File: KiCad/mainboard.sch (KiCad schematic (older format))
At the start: 60 parts, among them J1 Arduino_Nano_Header, P1 CONN_02X13, P2 CONN_02X13, P3 USB_B, P4 CONN_01X04, P5 CONN_01X02, P6 CONN_01X02, P7 CONN_01X02, U1 74LS165, U2 74LS165, U3 7400, U4 74LS595, U5 74LS595, U6 74LS595, U7 74LS595

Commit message: some changes and improvments
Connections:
- net GND: now also P3.5 (shield)
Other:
- moved on the sheet: P5, P6, P7

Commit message: added some metainfo
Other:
- note removed: "Podregilo main board"
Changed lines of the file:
@@
 encoding utf-8
 Sheet 1 1
-Title ""
+Title "Podregilo mainboard"
 Date ""
 Rev ""
-Comp ""
+Comp "https://github.com/johannes-mueller/Podregilo"
 Comment1 ""
 Comment2 ""
@@
 	1    0    0    -1
 $EndComp
-Text Notes 8350 7500 2    60   ~ 0
-Podregilo main board
 $Comp
 L GND #PWR07

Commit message: Added four missing LED-resistors and ...
... turned Arduino again. That was necessary because the connector must not be
at the edge of the PCB.
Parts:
- added R52, R53, R54, R55: 1k, Resistors_ThroughHole:Resistor_Horizontal_RM7mm, symbol R
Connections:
- net at P2.17 (P17): now also R55.2; no longer J1.14 (D11/MOSI)
- net at P2.19 (P19): now also R54.2; no longer J1.13 (D10/SS)
- net at P2.21 (P21): now also R53.2; no longer J1.12 (D9/0C1)
- net at P2.23 (P23): now also R52.2; no longer J1.11 (D8/ICP)
- new net: J1.11 (D8/ICP), R52.1
- new net: J1.12 (D9/0C1), R53.1
- new net: J1.13 (D10/SS), R54.1
- new net: J1.14 (D11/MOSI), R55.1
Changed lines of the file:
@@
 	800  6500 1000 6500
 Wire Wire Line
-	800  5100 800  6500
-Wire Wire Line
-	800  6500 800  7550
+	800  5100 800  7550
 Wire Wire Line
 	1000 5100 800  5100
@@
 	750  5400 1000 5400
 Wire Wire Line
-	750  5400 750  6800
-Wire Wire Line
-	750  6800 750  7600
+	750  5400 750  7600
 Wire Wire Line
 	750  6800 1000 6800
@@
 	4800 2550 4800 750
 Wire Wire Line
-	2200 2550 4250 2550
-Wire Wire Line
-	4250 2550 4800 2550
+	2200 2550 4800 2550
 Wire Wire Line
 	4250 2300 4250 2550
@@
 	4700 2500 4700 650
 Wire Wire Line
-	2350 2500 4400 2500
-Wire Wire Line
-	4400 2500 4700 2500
+	2350 2500 4700 2500
 Wire Wire Line
 	4400 2300 4400 2500
@@
 	7400 1350 7400 3700
 Wire Wire Line
-	5150 1850 5150 2750
-Wire Wire Line
-	5150 2750 5150 3800
+	5150 1850 5150 3800
 Wire Wire Line
 	5150 1850 5550 1850
 Wire Wire Line
-	3700 2850 4000 2850
-Wire Wire Line
-	4000 2850 5350 2850
-Wire Wire Line
-	5350 2850 5550 2850
+	3700 2850 5550 2850
 Wire Wire Line
 	5250 2350 5550 2350
 Wire Wire Line
-	5250 2350 5250 2800
-Wire Wire Line
-	5250 2800 5250 3900
+	5250 2350 5250 3900
 Wire Wire Line
 	5050 1350 5550 1350
 Wire Wire Line
-	5050 1350 5050 2700
-Wire Wire Line
-	5050 2700 5050 3700
+	5050 1350 5050 3700
 Connection ~ 5550 2850
 Connection ~ 5550 2350
@@
 Connection ~ 5550 1350
 Wire Wire Line
-	5550 2750 5550 2850
-Wire Wire Line
-	5550 2850 5550 2950
-Wire Wire Line
-	5550 2250 5550 2350
-Wire Wire Line
-	5550 2350 5550 2450
-Wire Wire Line
-	5550 1750 5550 1850
-Wire Wire Line
-	5550 1850 5550 1950
-Wire Wire Line
-	5550 1250 5550 1350
-Wire Wire Line
-	5550 1350 5550 1450
+	5550 2750 5550 2950
+Wire Wire Line
+	5550 2250 5550 2450
+Wire Wire Line
+	5550 1750 5550 1950
+Wire Wire Line
+	5550 1250 5550 1450
 Wire Wire Line
 	2800 2300 3300 2300
@@
 	1350 900  1350 800
 Wire Wire Line
-	1950 2300 1950 3000
-Wire Wire Line
-	1950 3000 1950 3200
-Wire Wire Line
-	1850 2300 1850 2950
-Wire Wire Line
-	1850 2950 1850 3200
-Wire Wire Line
-	1750 2300 1750 2900
-Wire Wire Line
-	1750 2900 1750 3200
-Wire Wire Line
-	1650 2300 1650 2850
-Wire Wire Line
-	1650 2850 1650 3200
-Wire Wire Line
-	1550 2300 1550 2800
-Wire Wire Line
-	1550 2800 1550 3200
-Wire Wire Line
-	1450 2300 1450 2750
-Wire Wire Line
-	1450 2750 1450 3200
-Wire Wire Line
-	1350 2300 1350 2700
-Wire Wire Line
-	1350 2700 1350 3200
+	1950 2300 1950 3200
+Wire Wire Line
+	1850 2300 1850 3200
+Wire Wire Line
+	1750 2300 1750 3200
+Wire Wire Line
+	1650 2300 1650 3200
+Wire Wire Line
+	1550 2300 1550 3200
+Wire Wire Line
+	1450 2300 1450 3200
+Wire Wire Line
+	1350 2300 1350 3200
 Wire Wire Line
 	5250 6600 5350 6600
@@
 	9250 4400 9350 4400
 Wire Wire Line
-	5700 7550 5700 6500
-Wire Wire Line
-	5700 6500 5700 5300
+	5700 7550 5700 5300
 Wire Wire Line
 	5700 5300 9600 5300
@@
 	9250 4300 9600 4300
 Wire Wire Line
-	9600 5300 9600 4300
-Wire Wire Line
-	9600 4300 9600 3200
+	9600 5300 9600 3200
 Wire Wire Line
 	9600 3200 10200 3200
 Wire Wire Line
-	9700 3300 9700 4600
-Wire Wire Line
-	9700 4600 9700 5400
+	9700 3300 9700 5400
 Wire Wire Line
 	9700 3300 10200 3300
 Connection ~ 9600 4300
 Wire Wire Line
-	5800 7600 5800 6800
-Wire Wire Line
-	5800 6800 5800 5400
+	5800 7600 5800 5400
 Wire Wire Line
 	5800 5400 9700 5400
@@
 	7400 1350 7050 1350
 Wire Wire Line
-	3400 2300 3400 2700
-Wire Wire Line
-	3400 2700 3400 3200
-Wire Wire Line
-	3500 2300 3500 2750
-Wire Wire Line
-	3500 2750 3500 3200
-Wire Wire Line
-	3600 2300 3600 2800
-Wire Wire Line
-	3600 2800 3600 3200
-Wire Wire Line
-	3700 2300 3700 2850
-Wire Wire Line
-	3700 2850 3700 3200
+	3400 2300 3400 3200
+Wire Wire Line
+	3500 2300 3500 3200
+Wire Wire Line
+	3600 2300 3600 3200
+Wire Wire Line
+	3700 2300 3700 3200
 Wire Wire Line
 	3400 3650 3400 3500
@@
 Connection ~ 3700 3650
 Wire Wire Line
-	3800 2300 3900 2300
-Wire Wire Line
-	3900 2300 4000 2300
-Wire Wire Line
-	4000 2300 4100 2300
+	3800 2300 4100 2300
 Connection ~ 3900 2300
 Connection ~ 4000 2300
@@
 	1350 3500 1350 3650
 Wire Wire Line
-	1350 3650 1450 3650
-Wire Wire Line
-	1450 3650 1550 3650
-Wire Wire Line
-	1550 3650 1650 3650
-Wire Wire Line
-	1650 3650 1750 3650
-Wire Wire Line
-	1750 3650 1850 3650
-Wire Wire Line
-	1850 3650 1950 3650
-Wire Wire Line
-	1950 3650 3400 3650
-Wire Wire Line
-	3400 3650 3500 3650
-Wire Wire Line
-	3500 3650 3600 3650
-Wire Wire Line
-	3600 3650 3700 3650
+	1350 3650 3700 3650
 Wire Wire Line
 	6500 4100 2650 4100
@@
 Connection ~ 3400 2700
 Wire Wire Line
-	3500 2750 4700 2750
-Wire Wire Line
-	4700 2750 5150 2750
+	3500 2750 5150 2750
 Connection ~ 5150 2750
 Connection ~ 3500 2750
 Wire Wire Line
-	3600 2800 4350 2800
-Wire Wire Line
-	4350 2800 5250 2800
+	3600 2800 5250 2800
 Connection ~ 5250 2800
 Connection ~ 3600 2800
@@
 Connection ~ 4700 2750
 Wire Wire Line
-	4100 3500 4450 3500
-Wire Wire Line
-	4450 3500 4800 3500
+	4100 3500 4800 3500
 Connection ~ 4450 3500
 $Comp
@@
 	3750 5900 3750 5800
 Wire Wire Line
-	3750 5800 9800 5800
-Wire Wire Line
 	9800 5800 9800 3400
 Wire Wire Line
 	9900 3500 9900 5900
 Wire Wire Line
-	9900 5900 3850 5900
-Wire Wire Line
 	3850 5900 3850 6000
 Wire Wire Line
@@
 	10000 3600 10000 6000
 Wire Wire Line
-	10000 6000 3950 6000
-Wire Wire Line
 	3950 6000 3950 6100
 Wire Wire Line
@@
 	10100 3700 10100 6100
 Wire Wire Line
-	10100 6100 4050 6100
-Wire Wire Line
 	4050 6100 4050 6200
 Wire Wire Line
 	4050 6200 3500 6200
+$Comp
+L R R52
+U 1 1 587072D5
+P 9500 5800
+F 0 "R52" V 9450 5650 50  0000 C CNN
+F 1 "1k" V 9500 5800 50  0000 C CNN
+F 2 "Resistors_ThroughHole:Resistor_Horizontal_RM7mm" H 9430 5800 50  0001 C CNN
+F 3 "" H 9500 5800 50  0000 C CNN
+	1    9500 5800
+	0    1    1    0
+$EndComp
+$Comp
+L R R53
+U 1 1 5870767C
+P 9500 5900
+F 0 "R53" V 9450 5750 50  0000 C CNN
+F 1 "1k" V 9500 5900 50  0000 C CNN
+F 2 "Resistors_ThroughHole:Resistor_Horizontal_RM7mm" V 9430 5900 50  0001 C CNN
+F 3 "" H 9500 5900 50  0000 C CNN
+	1    9500 5900
+	0    1    1    0
+$EndComp
+$Comp
+L R R54
+U 1 1 58707841
+P 9500 6000
+F 0 "R54" V 9450 5850 50  0000 C CNN
+F 1 "1k" V 9500 6000 50  0000 C CNN
+F 2 "Resistors_ThroughHole:Resistor_Horizontal_RM7mm" V 9430 6000 50  0001 C CNN
+F 3 "" H 9500 6000 50  0000 C CNN
+	1    9500 6000
+	0    1    1    0
+$EndComp
+$Comp
+L R R55
+U 1 1 587078A3
+P 9500 6100
+F 0 "R55" V 9450 5950 50  0000 C CNN
+F 1 "1k" V 9500 6100 50  0000 C CNN
+F 2 "Resistors_ThroughHole:Resistor_Horizontal_RM7mm" V 9430 6100 50  0001 C CNN
+F 3 "" H 9500 6100 50  0000 C CNN
+	1    9500 6100
+	0    1    1    0
+$EndComp
+Wire Wire Line
+	9650 5800 9800 5800
+Wire Wire Line
+	9900 5900 9650 5900
+Wire Wire Line
+	10000 6000 9650 6000
+Wire Wire Line
+	10100 6100 9650 6100
+Wire Wire Line
+	3750 5800 9350 5800
+Wire Wire Line
+	3850 5900 9350 5900
+Wire Wire Line
+	3950 6000 9350 6000
+Wire Wire Line
+	4050 6100 9350 6100
 $EndSCHEMATC

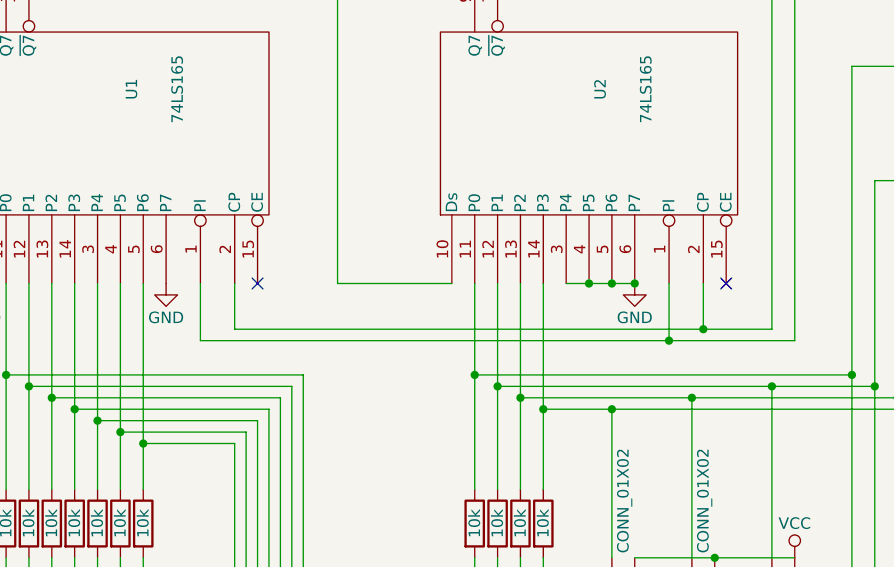
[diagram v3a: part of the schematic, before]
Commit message: Made CLK INH (Pin 15) of the 74HC165s LO
The input shift registers turned out to have a strong tendency to disturbance
and their signals were very unstable. The manual of 74HC165 says, that all
the unused input pins should be either at GND or VCC. For the CLK INH
(clock inhibit) VCC is not an option, as this would inhibit the clock.
Therefore we put them to GND.

It turns out to be far more stable.
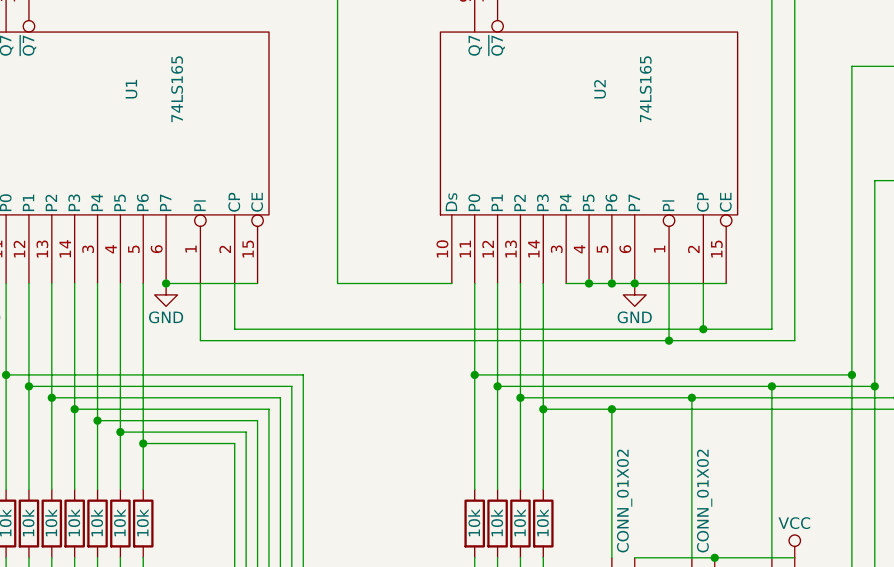
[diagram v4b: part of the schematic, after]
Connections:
- net GND: now also U1.15 (CE), U2.15 (CE)
- no-connect marks 26 -> 24

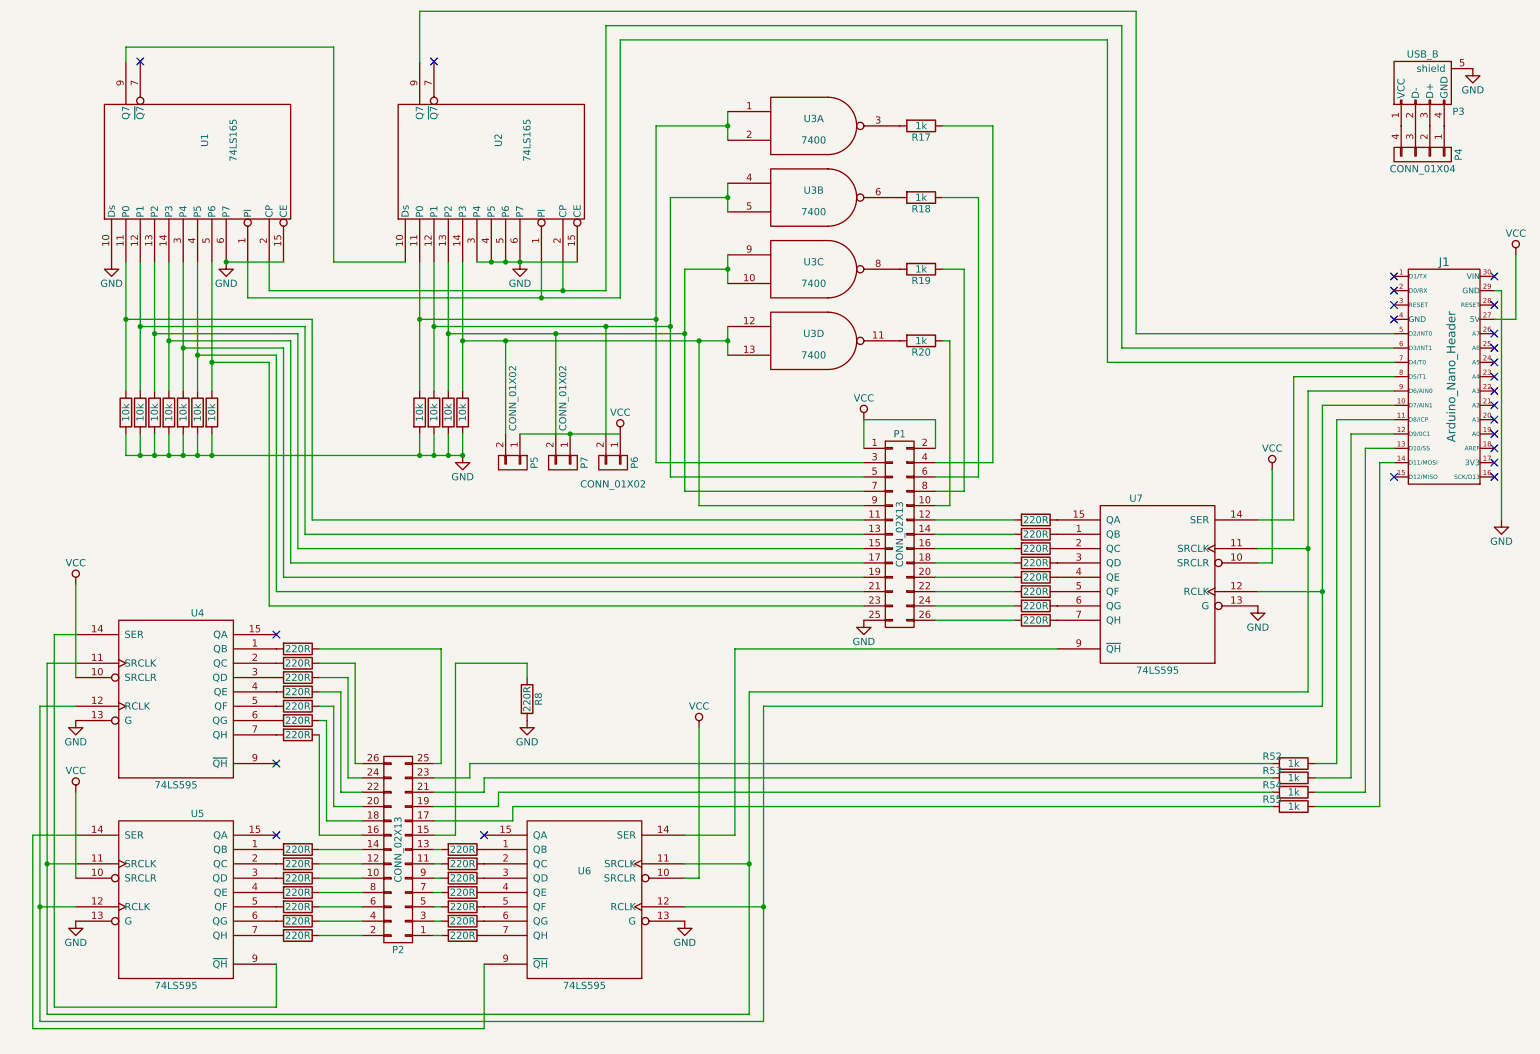
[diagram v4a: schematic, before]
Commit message: Added decoupling capacitors to the ICs
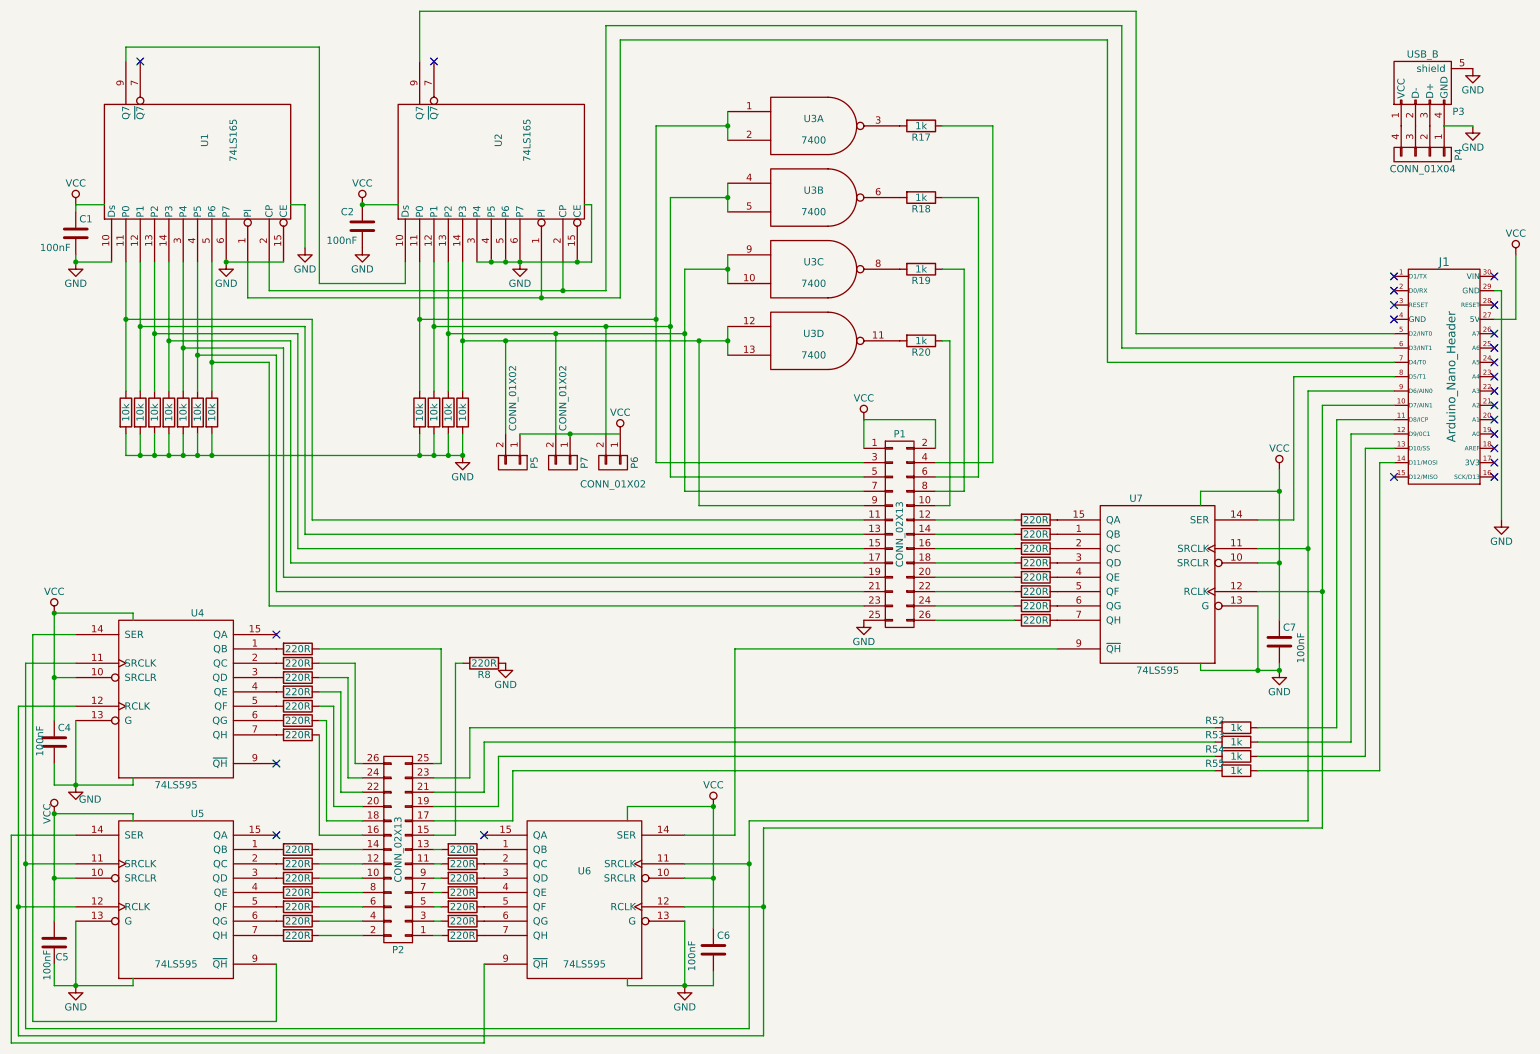
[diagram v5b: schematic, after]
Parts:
- added C1, C2, C4, C5, C6, C7: 100nF, Capacitors_ThroughHole:C_Disc_D3_P2.5, symbol C
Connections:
- net GND: now also P3.4 (GND), P4.1 (P1), R8.1, C1.2, C2.2, C4.2, C5.1, C6.2, C7.2; no longer R8.2
- net VCC: now also C1.1, C2.1, C4.1, C5.2, C6.1, C7.1
- net at P2.15 (P15): now also R8.2; no longer R8.1
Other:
- moved on the sheet: R52, R53, R54, R55, R8

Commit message: KiCad update; wiring of denoising capacitors
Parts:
- C1, C2, C4, C5, C6, C7: symbol C -> mainboard-rescue:C
- J1: symbol Arduino_Nano_Header -> mainboard-rescue:Arduino_Nano_Header
- P1, P2: symbol CONN_02X13 -> mainboard-rescue:CONN_02X13
- P3: symbol USB_B -> mainboard-rescue:USB_B-RESCUE-mainboard
- P4: symbol CONN_01X04 -> mainboard-rescue:CONN_01X04
- P5, P6, P7: symbol CONN_01X02 -> mainboard-rescue:CONN_01X02
- R1, R13, R14, R15, R16, R17, R18, R19, R2, R20, R21, R22, R23, R24, R25, R26, R27, R29, R3, R30, R31, R32, R33, R34, R35, R37, R38, R39, R4, R40, R41, R42, R43, R44, R45, R46, R47, R48, R49, R5, R50, R51, R52, R53, R54, R55, R6, R7, R8: symbol R -> mainboard-rescue:R
- U1, U2: symbol 74LS165 -> mainboard-rescue:74LS165
- U3: symbol 7400 -> mainboard-rescue:7400
- U4, U5, U6, U7: symbol 74LS595 -> mainboard-rescue:74LS595
